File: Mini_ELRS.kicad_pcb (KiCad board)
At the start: 4 copper layers, 27.9 x 26.9 mm, 24 parts, among them J1 Conn_01x06, J2 Conn_01x06, J3 Conn_01x06, SW1 SW_Push, U1 ESP32-PICO-D4, U2 TC2014-3.3VxCTTR, U3 SX1280IMLTRT, Y1 Crystal_GND24_Small

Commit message: update esp32_with_mos
Signed-off-by: huangzzk <huangcmzzk@gmail.com>
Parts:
- added J4: Conn_01x03_MountingPin, Connector_Molex:Molex_CLIK-Mate_502386-0370_1x03-1MP_P1.25mm_Horizontal, B.Cu at (119.8, 68.4)
- added J5: Conn_01x03, Connector_Molex:Molex_CLIK-Mate_502386-0370_1x03-1MP_P1.25mm_Horizontal, B.Cu at (111.6, 68.4)
- added J6: Conn_01x03_MountingPin, Connector_Molex:Molex_CLIK-Mate_502386-0370_1x03-1MP_P1.25mm_Horizontal, B.Cu at (115.1, 59.1)
- added Q1: Q_NMOS_GSD, Package_TO_SOT_SMD:SOT-23, B.Cu at (106.3, 64.0)
- added Q2: Q_NMOS_GSD, Package_TO_SOT_SMD:SOT-23, B.Cu at (110.0, 61.3)
- added R4: 10K, Resistor_SMD:R_0402_1005Metric, B.Cu at (106.6, 70.4)
- added R5: 10K, Resistor_SMD:R_0402_1005Metric, B.Cu at (103.9, 61.3)
- C1, R1: moved to B.Cu
- J1, J2: value Conn_01x06 -> Conn_01x03_MountingPin; footprint Connector_PinHeader_2.54mm:PinHeader_1x06_P2.54mm_Vertical -> Connector_Molex:Molex_CLIK-Mate_502386-0370_1x03-1MP_P1.25mm_Horizontal; moved to B.Cu
- J3: value Conn_01x06 -> Conn_01x04; footprint Connector_PinHeader_2.54mm:PinHeader_1x06_P2.54mm_Vertical -> Connector_PinHeader_2.54mm:PinHeader_1x04_P2.54mm_Vertical
- moved R1 17.8 mm to (122.3, 64.4), turned to 180 degrees
- moved J1 13.3 mm to (104.3, 67.5), turned to 90 degrees
- moved C1 12.3 mm to (119.3, 64.4), turned to 180 degrees
- moved J2 6.82 mm to (106.6, 59.1), turned to 0 degrees
- moved D2 6.79 mm to (110.1, 57.6)
- moved R3 6.64 mm to (111.7, 57.6)
- moved D1 4.73 mm to (116.5, 70.3)
- moved J3 4.59 mm to (102.0, 60.6)
- moved SW1 2.32 mm to (106.5, 57.8), turned to 180 degrees
- moved U1 1.66 mm to (108.0, 63.8)
- moved R2 1.49 mm to (119.5, 70.3)
- moved C9 1.03 mm to (114.9, 68.3)
- moved C7 1.03 mm to (114.9, 66.8)
- moved C3 0.37 mm to (122.5, 70.3)
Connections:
- C2 pad 1: +5V -> +BATT
- J1 pad 1: Net-(J1-Pad1) -> /PWM1
- J1 pad 2: Net-(J1-Pad2) -> +BATT
- J1 pad 3: Net-(J1-Pad3) -> Net-(Q1-Pad3)
- J2 pad 1: Net-(J2-Pad1) -> /PWM2
- J2 pad 2: Net-(J2-Pad2) -> +BATT
- J2 pad 3: /MISO -> Net-(Q2-Pad3)
- J3 pad 1: unconnected-(J3-Pad1) -> +BATT
- J3 pad 2: unconnected-(J3-Pad2) -> /RX
- J3 pad 3: /RX -> /TX
- J3 pad 4: /TX -> GND
- U1 pad 10: Net-(J1-Pad5) -> unconnected-(U1-Pad10)
- U1 pad 12: Net-(J1-Pad3) -> /PWM7
- U1 pad 13: Net-(J1-Pad4) -> /PWM4
- U1 pad 14: unconnected-(U1-Pad14) -> /PWM3
- U1 pad 15: Net-(J1-Pad1) -> unconnected-(U1-Pad15)
- U1 pad 16: Net-(J1-Pad2) -> /MOSI
- U1 pad 17: /SCK -> unconnected-(U1-Pad17)
- U1 pad 18: /MISO -> /SCK
- U1 pad 20: /MOSI -> /NSS
- U1 pad 21: /NSS -> unconnected-(U1-Pad21)
- U1 pad 22: /NRST -> /LED
- U1 pad 24: /DIO1 -> /NRST
- U1 pad 28: Net-(J2-Pad1) -> /PWM5
- U1 pad 29: Net-(J2-Pad2) -> unconnected-(U1-Pad29)
- U1 pad 34: /BUSY -> /PWM2
- U1 pad 35: /LED -> unconnected-(U1-Pad35)
- U1 pad 36: unconnected-(U1-Pad36) -> /PWM6
- U1 pad 39: unconnected-(U1-Pad39) -> /PWM1
- U1 pad 42: unconnected-(U1-Pad42) -> /PWM8
- U1 pad 5: unconnected-(U1-Pad5) -> /BUSY
- U1 pad 7: unconnected-(U1-Pad7) -> /DIO1
- U1 pad 8: unconnected-(U1-Pad8) -> /MISO
- U2 pad 1: +5V -> +BATT
- U2 pad 3: +5V -> +BATT
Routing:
- net +5V: track 28.5 -> 0.00 mm, vias 1 -> 0
- net /ESP32_ANT: track 4.50 -> 30.7 mm
- net /SCK: track 27.3 -> 6.91 mm, vias 1 -> 2
- net /NSS: track 21.6 -> 7.17 mm, vias 3 -> 2
- net /MOSI: track 20.5 -> 6.14 mm
- net +BATT: track 0.00 -> 13.1 mm, vias 0 -> 8
- net Net-(C1-Pad1): track 3.65 -> 15.6 mm, vias 0 -> 2
- net /PWM1: track 0.00 -> 11.8 mm, vias 0 -> 1
- net Net-(J2-Pad1): track 11.6 -> 0.00 mm, vias 2 -> 0
- net /PWM3: track 0.00 -> 11.3 mm, vias 0 -> 1
- net /MISO: track 21.6 -> 10.8 mm, vias 1 -> 2
- net /PWM2: track 0.00 -> 10.8 mm, vias 0 -> 2
- net GND: track 14.5 -> 24.6 mm, vias 15 -> 16
- net Net-(J2-Pad2): track 9.26 -> 0.00 mm, vias 1 -> 0
- net Net-(J1-Pad1): track 9.05 -> 0.00 mm, vias 1 -> 0
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- added copper zone on In2.Cu, net +BATT
- removed copper zone on In2.Cu, net GND
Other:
- board size 27.9 x 26.9 mm -> 22.9 x 15.8 mm
- board text added: "+"
- board text added: "G"
- board text added: "PWM1"
- board text added: "PWM2"
- board text added: "PWM3"
- board text added: "PWM4"
- board text added: "PWM5"
- board text added: "R"
- board text added: "T"
- board text removed: "5V"
- board text removed: "ANT"
- board text removed: "GND"
- board text removed: "MI"
- board text removed: "MO"
- board text removed: "NSS"
- board text removed: "RX"
- board text removed: "SCK"
- board text removed: "TX"

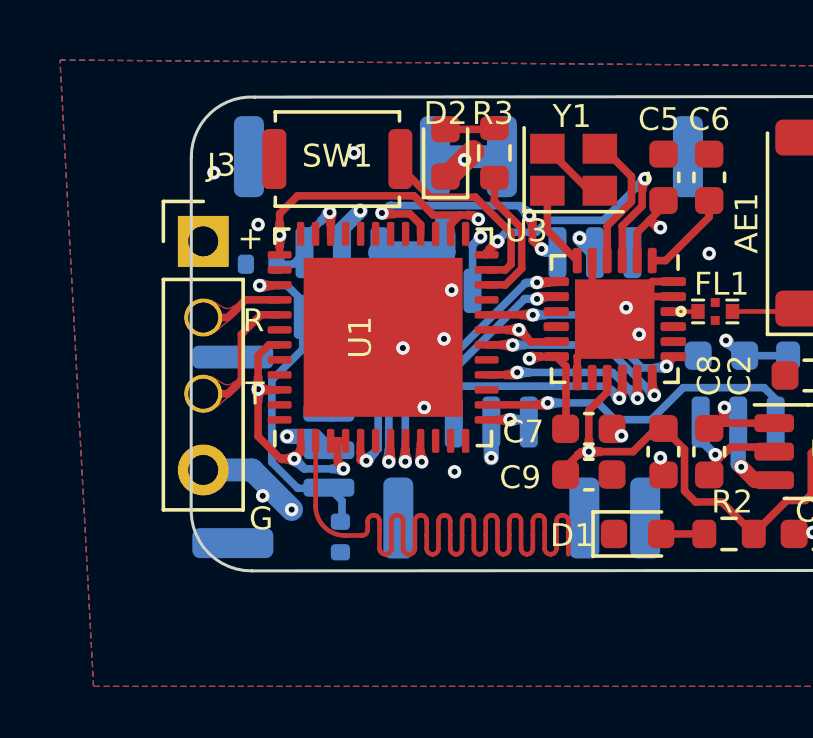
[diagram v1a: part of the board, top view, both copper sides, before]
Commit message: fix the 2.54 connector package.
Signed-off-by: huangzzk <huangcmzzk@gmail.com>
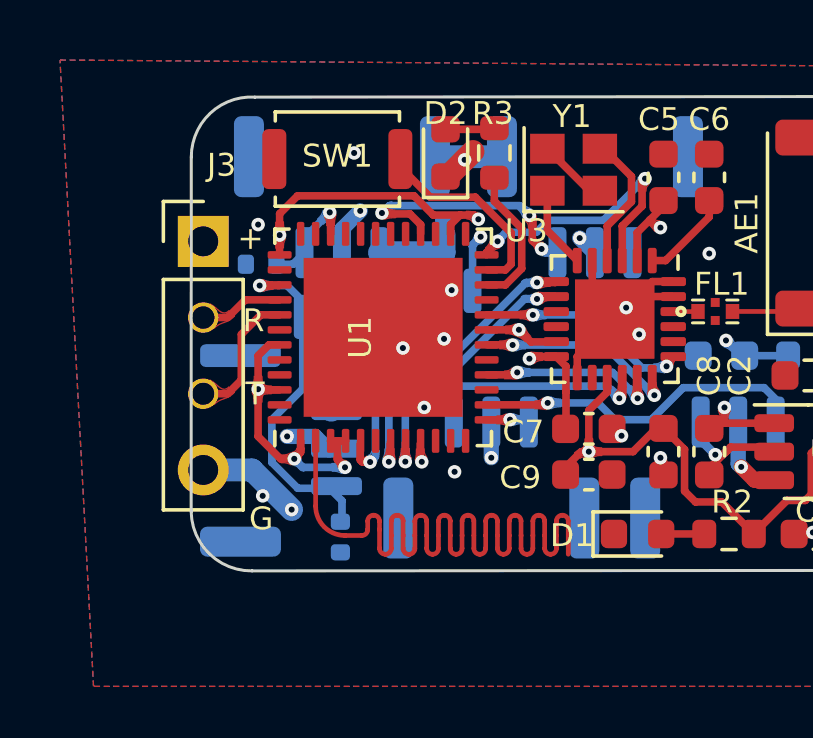
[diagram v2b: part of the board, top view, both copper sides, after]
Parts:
- moved J1 0.26 mm to (104.6, 67.5)
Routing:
- net +BATT: vias 8 -> 7

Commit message: swap some pwm pins net name
Signed-off-by: huangzzk <huangcmzzk@gmail.com>
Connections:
- J1 pad 1: /PWM1 -> /PWM5
- J2 pad 1: /PWM2 -> /PWM3
- J4 pad 1: /PWM3 -> /PWM2
- J6 pad 1: /PWM5 -> /PWM1
- Q1 pad 1: /PWM1 -> /PWM5
- Q2 pad 1: /PWM2 -> /PWM3
- R4 pad 1: /PWM1 -> /PWM5
- R5 pad 1: /PWM2 -> /PWM3
- U1 pad 14: /PWM3 -> /PWM2
- U1 pad 28: /PWM5 -> /PWM1
- U1 pad 34: /PWM2 -> /PWM3
- U1 pad 39: /PWM1 -> /PWM5
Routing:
- net /PWM5: track 8.78 -> 11.8 mm, vias 3 -> 1
- net /PWM1: track 11.8 -> 8.78 mm, vias 1 -> 3
- net /PWM3: track 11.3 -> 10.8 mm, vias 1 -> 2
- net /PWM2: track 10.8 -> 11.3 mm, vias 2 -> 1

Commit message: remove something unncessary
Signed-off-by: huangzzk <huangcmzzk@gmail.com>
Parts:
- removed D1: LED, LED_SMD:LED_0603_1608Metric
- removed SW1: SW_Push, Button_Switch_SMD:SW_Push_SPST_NO_Alps_SKRK
- added R6: 10K, Resistor_SMD:R_0603_1608Metric, F.Cu at (134.3, 63.3)
- J1: value Conn_01x03_MountingPin -> Conn_01x02; footprint Connector_Molex:Molex_CLIK-Mate_502386-0370_1x03-1MP_P1.25mm_Horizontal -> Connector_PinHeader_2.54mm:PinHeader_2x01_P2.54mm_Vertical
- J5: value Conn_01x03 -> Conn_01x03_MountingPin
- R2: value 10K -> NC
- R4, R5: footprint Resistor_SMD:R_0402_1005Metric -> Resistor_SMD:R_0603_1608Metric
- moved R4 8.13 mm to (102.9, 63.1), turned to 180 degrees
- moved R5 4.71 mm to (108.0, 63.7)
- moved J5 3.83 mm to (107.8, 68.8)
- moved J3 2.03 mm to (100.0, 60.6)
- moved J2 1.98 mm to (104.6, 59.1)
- moved J1 1.96 mm to (102.7, 67.8)
- moved J4 0.93 mm to (119.0, 68.8)
- moved J6 0.76 mm to (115.8, 59.1)
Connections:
- J1 pad 1: /PWM5 -> +BATT
- J1 pad 2: +BATT -> Net-(Q1-Pad3)
- J5 pad MP: (no net) -> GND
- Q1 pad 3: Net-(J1-Pad3) -> Net-(Q1-Pad3)
- R2 pad 1: Net-(D1-Pad2) -> Net-(U1-Pad23)
- R2 pad 2: +3V3 -> GND
- U1 pad 23: Net-(SW1-Pad1) -> Net-(U1-Pad23)
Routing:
- net +3V3: track 59.4 -> 42.9 mm, vias 8 -> 6
- net Net-(C1-Pad1): track 15.6 -> 1.45 mm, vias 2 -> 0
- net /PWM2: track 11.3 -> 0.00 mm, vias 1 -> 0
- net GND: track 24.6 -> 13.6 mm, vias 16 -> 3
- net /MISO: track 10.8 -> 0.00 mm, vias 2 -> 0
- net /BUSY: track 10.6 -> 0.00 mm, vias 2 -> 0
- net +BATT: track 13.1 -> 2.52 mm, vias 7 -> 1
- net /DIO1: track 9.57 -> 0.62 mm, vias 2 -> 0
- net /PWM1: track 8.78 -> 0.00 mm, vias 3 -> 0
- net /PWM5: track 11.8 -> 3.31 mm
- net Net-(C5-Pad1): track 12.5 -> 4.70 mm, vias 2 -> 0
- net /ESP32_ANT: track 30.7 -> 38.4 mm
- net Net-(SW1-Pad1): track 6.81 -> 0.00 mm
- net /TX: track 4.41 -> 0.00 mm
- net /PWM3: track 10.8 -> 8.01 mm
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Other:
- board size 22.9 x 15.8 mm -> 26.7 x 15.8 mm

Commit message: finished TX mobile
Signed-off-by: huangzzk <huangcmzzk@gmail.com>
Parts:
- removed C3: 180pF, Capacitor_SMD:C_0603_1608Metric
- removed J1: Conn_01x02, Connector_PinHeader_2.54mm:PinHeader_2x01_P2.54mm_Vertical
- removed J2, J4, J5, J6: Conn_01x03_MountingPin, Connector_Molex:Molex_CLIK-Mate_502386-0370_1x03-1MP_P1.25mm_Horizontal
- removed R2: NC, Resistor_SMD:R_0603_1608Metric
- added R7: 10K, Resistor_SMD:R_0603_1608Metric, F.Cu at (119.7, 69.7)
- added TP1: TestPoint, TestPoint:TestPoint_Pad_1.0x1.0mm, F.Cu at (110.1, 57.6)
- added U4: CH340E, Package_SO:MSOP-10_3x3mm_P0.5mm, B.Cu at (102.0, 67.7)
- added USB1: 918-118A2021Y40002, ic_footprint:TYPE-C-SMD_JINGTUOJIN_918-118A2021Y40002, F.Cu at (100.9, 64.3)
- C1, R1, R4, R5: moved to F.Cu
- moved R6 20.2 mm to (114.8, 68.5), turned to 180 degrees
- moved R1 8.58 mm to (116.8, 70.9), turned to 0 degrees
- moved R5 7.88 mm to (104.0, 70.5)
- moved R4 7.60 mm to (101.2, 70.6)
- moved C1 6.57 mm to (119.7, 70.9), turned to 0 degrees
- moved Q2 5.95 mm to (112.1, 66.9), turned to 0 degrees
- moved Q1 3.38 mm to (108.1, 66.9), turned to 0 degrees
- moved J3 2.95 mm to (100.2, 57.7), turned to 90 degrees
- moved C9 2.33 mm to (116.7, 69.7)
- moved D2 1.79 mm to (111.9, 57.4)
- moved R3 1.63 mm to (113.3, 57.6)
- moved Y1 1.61 mm to (115.8, 57.4)
- moved C5 1.30 mm to (118.2, 57.5)
- moved C6 1.30 mm to (119.7, 57.5)
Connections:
- net +BATT renamed +5V
- Q1 pad 1: /PWM5 -> /CRSF_TX
- Q2 pad 1: /PWM3 -> Net-(Q1-Pad3)
- Q2 pad 3: Net-(J2-Pad3) -> /CRSF
- R4 pad 1: /PWM5 -> GND
- R4 pad 2: GND -> Net-(R4-Pad2)
- R5 pad 1: /PWM3 -> Net-(R5-Pad1)
- R6 pad 1: /NSS -> Net-(Q1-Pad3)
- R6 pad 2: GND -> /TNOW
- U1 pad 12: /PWM7 -> unconnected-(U1-Pad12)
- U1 pad 13: /PWM4 -> unconnected-(U1-Pad13)
- U1 pad 14: /PWM2 -> unconnected-(U1-Pad14)
- U1 pad 16: /MOSI -> unconnected-(U1-Pad16)
- U1 pad 17: unconnected-(U1-Pad17) -> /NRST
- U1 pad 18: /SCK -> unconnected-(U1-Pad18)
- U1 pad 20: /NSS -> /CRSF
- U1 pad 21: unconnected-(U1-Pad21) -> /LED
- U1 pad 22: /LED -> unconnected-(U1-Pad22)
- U1 pad 24: /NRST -> /DIO1
- U1 pad 28: /PWM1 -> unconnected-(U1-Pad28)
- U1 pad 34: /PWM3 -> /NSS
- U1 pad 35: unconnected-(U1-Pad35) -> /SCK
- U1 pad 36: /PWM6 -> /MOSI
- U1 pad 38: unconnected-(U1-Pad38) -> /MISO
- U1 pad 39: /PWM5 -> unconnected-(U1-Pad39)
- U1 pad 42: /PWM8 -> /BUSY
- U1 pad 5: /BUSY -> unconnected-(U1-Pad5)
- U1 pad 7: /DIO1 -> unconnected-(U1-Pad7)
- U1 pad 8: /MISO -> unconnected-(U1-Pad8)
- U2 pad 4: Net-(C3-Pad1) -> unconnected-(U2-Pad4)
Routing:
- net +5V: track 2.52 -> 49.1 mm, vias 1 -> 2
- net +3V3: track 42.9 -> 72.1 mm, vias 6 -> 11
- net /CRSF: track 0.00 -> 24.4 mm, vias 0 -> 4
- net /MISO: track 0.00 -> 17.1 mm, vias 0 -> 2
- net /MOSI: track 6.14 -> 19.0 mm
- net /TNOW: track 0.00 -> 12.5 mm, vias 0 -> 1
- net /SCK: track 6.91 -> 18.7 mm
- net /BUSY: track 0.00 -> 11.7 mm, vias 0 -> 2
- net Net-(C5-Pad1): track 4.70 -> 15.8 mm, vias 0 -> 2
- net Net-(C1-Pad1): track 1.45 -> 12.2 mm, vias 0 -> 2
- net /NSS: track 7.17 -> 17.6 mm
- net Net-(R4-Pad2): track 0.00 -> 9.32 mm, vias 0 -> 2
- net /PWM3: track 8.01 -> 0.00 mm, vias 2 -> 0
- net /DP: track 0.00 -> 7.89 mm, vias 0 -> 2
- net Net-(Q1-Pad3): track 0.00 -> 7.64 mm, vias 0 -> 1
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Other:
- board size 26.7 x 15.8 mm -> 26.5 x 16.1 mm
- board text removed: "PWM1"
- board text removed: "PWM2"
- board text removed: "PWM3"
- board text removed: "PWM4"
- board text removed: "PWM5"

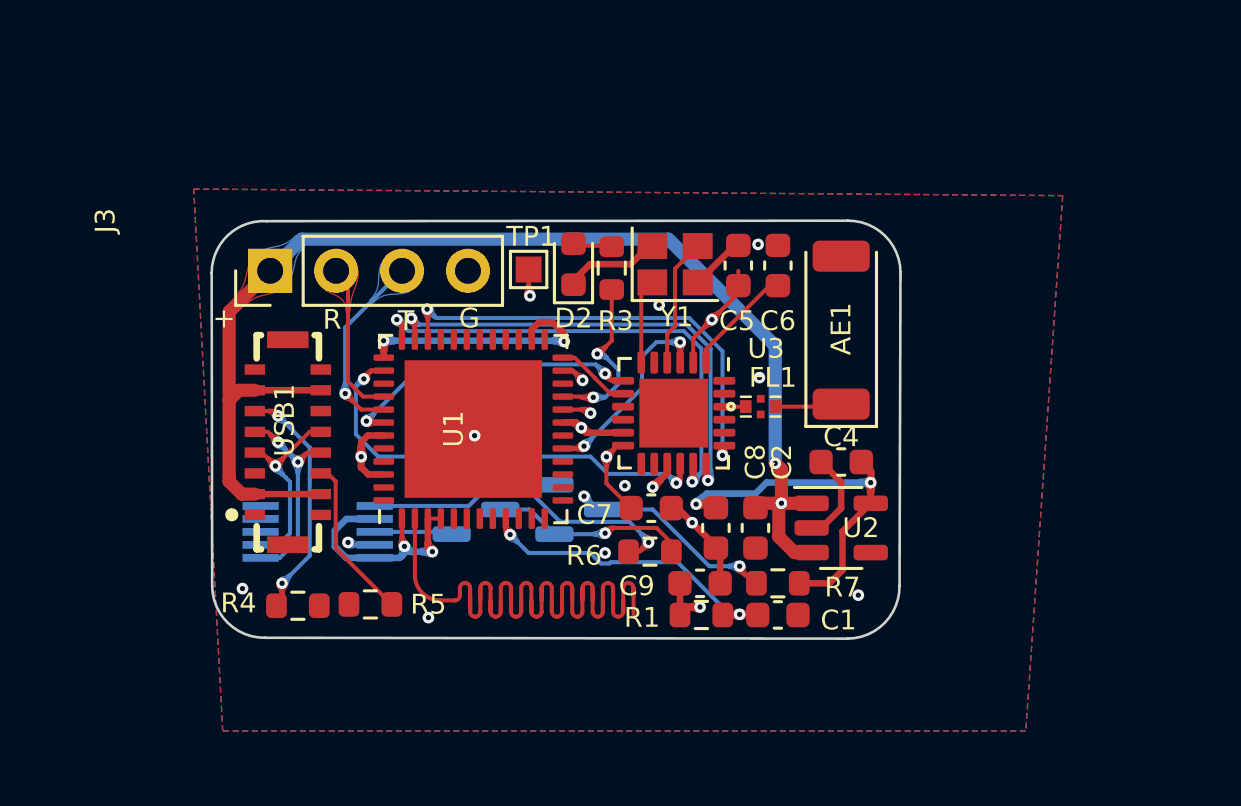
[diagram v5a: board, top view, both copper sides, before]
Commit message: use another Type-c package
Signed-off-by: huangzzk <huangcmzzk@gmail.com>
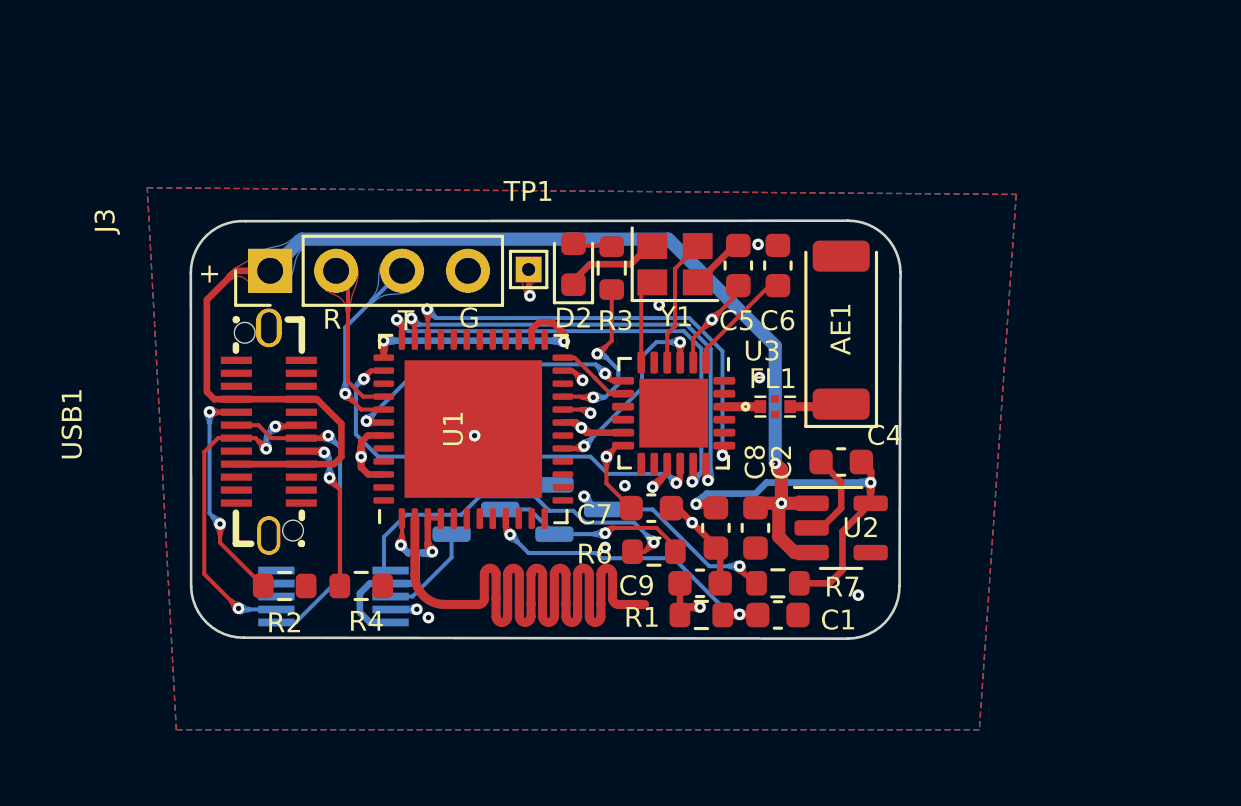
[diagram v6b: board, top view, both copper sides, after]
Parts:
- removed R5: 10K, Resistor_SMD:R_0603_1608Metric
- added R2: 5.1K, Resistor_SMD:R_0603_1608Metric, F.Cu at (100.7, 69.8)
- R4: value 10K -> 5.1K
- R6, R7: value 10K -> 1K
- TP1: footprint TestPoint:TestPoint_Pad_1.0x1.0mm -> TestPoint:TestPoint_THTPad_1.0x1.0mm_Drill0.5mm
- USB1: value 918-118A2021Y40002 -> U263-241N-4BQC15; footprint ic_footprint:TYPE-C-SMD_JINGTUOJIN_918-118A2021Y40002 -> ic_footprint:USB-C-SMD_U263-241N-4BQC15
- moved U4 2.56 mm to (102.6, 70.2)
- moved R4 2.55 mm to (103.7, 69.8), turned to 0 degrees
- moved USB1 0.84 mm to (100.1, 63.9)
- moved FL1 0.56 mm to (119.6, 62.9)
- moved R6 0.15 mm to (115.0, 68.5)
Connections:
- R4 pad 1: GND -> Net-(R4-Pad1)
- R4 pad 2: Net-(R4-Pad2) -> GND
- USB1 pad 10: +5V -> unconnected-(USB1-Pad10)
- USB1 pad 11: Net-(R5-Pad1) -> unconnected-(USB1-Pad11)
- USB1 pad 12: /DP -> GND
- USB1 pad 13: /DN -> GND
- USB1 pad 15: +5V -> unconnected-(USB1-Pad15)
- USB1 pad 16: GND -> +5V
- USB1 pad 17: GND -> Net-(R4-Pad1)
- USB1 pad 18: GND -> /DP
- USB1 pad 2: +5V -> unconnected-(USB1-Pad2)
- USB1 pad 4: /DN -> +5V
- USB1 pad 5: /DP -> Net-(R2-Pad2)
- USB1 pad 6: Net-(R4-Pad2) -> /DP
- USB1 pad 7: +5V -> /DN
- USB1 pad 8: GND -> unconnected-(USB1-Pad8)
- USB1 pad 9: GND -> +5V
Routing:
- net Net-(R4-Pad2): track 9.32 -> 0.00 mm, vias 2 -> 0
- net Net-(R2-Pad2): track 0.00 -> 8.60 mm, vias 0 -> 2
- net Net-(R5-Pad1): track 6.34 -> 0.00 mm
- net Net-(R4-Pad1): track 0.00 -> 6.30 mm, vias 0 -> 2
- net /ESP32_ANT: track 38.4 -> 32.7 mm
- net /DN: track 7.44 -> 12.6 mm, vias 1 -> 3
- net /DP: track 7.89 -> 12.9 mm, vias 2 -> 1
- net /TNOW: track 12.5 -> 14.2 mm
- net +5V: track 49.1 -> 50.4 mm
- net /CRSF_TX: track 2.99 -> 4.13 mm
- net Net-(C5-Pad1): track 15.8 -> 15.2 mm
- net /RF: track 0.83 -> 1.39 mm
- net Net-(AE1-Pad1): track 2.57 -> 2.02 mm
- net GND: vias 9 -> 8
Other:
- board size 26.5 x 16.1 mm -> 27.3 x 16.1 mm
